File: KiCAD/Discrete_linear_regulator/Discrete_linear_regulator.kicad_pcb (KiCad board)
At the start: 2 copper layers, 50 x 30 mm, 14 parts, among them J1 Conn_01x06, Q1 PZT2222AT3G, Q2 BC857, Q3 BC857, Q4 PZT2222AT3G, Q5 PZT2907AT3G, Q6 BC847, Q7 BC847, Q8 PZT2907AT3G, U1 LM4562

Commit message: Worked a bit on the main board
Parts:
- added C1: 100nF, Capacitor_SMD:C_0402_1005Metric, B.Cu at (75.0, 64.0)
- added C3: 100nF, Capacitor_SMD:C_0402_1005Metric, B.Cu at (75.0, 66.0)
- moved Q6 90.0 mm to (97.1, 69.5)
- moved Q7 90.0 mm to (97.1, 74.0)
- moved C2 53.3 mm to (81.0, 63.0)
- moved Q2 52.8 mm to (62.0, 65.0), turned to 180 degrees
- moved R2 52.5 mm to (61.0, 72.0), turned to 90 degrees
- moved Q3 52.4 mm to (62.0, 69.0), turned to 90 degrees
- moved R1 49.3 mm to (65.0, 65.0), turned to -90 degrees
- moved C4 46.8 mm to (69.0, 66.0), turned to 180 degrees

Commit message: sepic step file
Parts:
- removed Q6, Q7: BC847, Package_TO_SOT_SMD:SOT-23
- added C10: 100u, Capacitor_THT:CP_Radial_D8.0mm_P3.50mm, F.Cu at (39.8, 92.3)
- added C11: 100u, Capacitor_THT:CP_Radial_D8.0mm_P3.50mm, F.Cu at (110.8, 56.0)
- added C12: 100u, Capacitor_THT:CP_Radial_D8.0mm_P3.50mm, F.Cu at (110.8, 65.5)
- added C13: 10u, Capacitor_SMD:C_1210_3225Metric, F.Cu at (38.1, 64.2)
- added C14: 100n, Capacitor_SMD:C_0402_1005Metric, F.Cu at (42.3, 62.7)
- added C15: 100p, Capacitor_SMD:C_0402_1005Metric, F.Cu at (42.3, 64.7)
- added C16: 100u, Capacitor_THT:CP_Radial_D8.0mm_P3.50mm, F.Cu at (110.8, 75.0)
- added C5: 100u, Capacitor_THT:CP_Radial_D8.0mm_P3.50mm, F.Cu at (39.8, 73.2)
- added C6: 100u, Capacitor_THT:CP_Radial_D8.0mm_P3.50mm, F.Cu at (39.8, 82.8)
- added C9: 10u, Capacitor_SMD:C_1210_3225Metric, F.Cu at (38.1, 59.9)
- added Q10: BC857, Package_TO_SOT_SMD:SOT-23, F.Cu at (37.7, 43.2)
- added Q11: BC857, Package_TO_SOT_SMD:SOT-23, F.Cu at (37.7, 47.6)
- added R10: 47R, Resistor_SMD:R_0402_1005Metric, F.Cu at (39.6, 56.8)
- added R11: 10k, Resistor_SMD:R_0402_1005Metric, F.Cu at (42.5, 50.8)
- added R12: 780R, Resistor_SMD:R_0402_1005Metric, F.Cu at (42.5, 52.8)
- added R13: 8k2, Resistor_SMD:R_0402_1005Metric, F.Cu at (42.5, 54.8)
- added R14: 2k4, Resistor_SMD:R_0402_1005Metric, F.Cu at (42.5, 56.8)
- added R3: 47R, Resistor_SMD:R_0402_1005Metric, F.Cu at (36.7, 50.8)
- added R4: 100R, Resistor_SMD:R_0402_1005Metric, F.Cu at (36.7, 52.8)
- added R5: 100k, Resistor_SMD:R_0402_1005Metric, F.Cu at (36.7, 54.8)
- added R6: 8k2, Resistor_SMD:R_0402_1005Metric, F.Cu at (36.7, 56.8)
- added R7: 2k4, Resistor_SMD:R_0402_1005Metric, F.Cu at (39.6, 50.8)
- added R8: 100R, Resistor_SMD:R_0402_1005Metric, F.Cu at (39.6, 52.8)
- added R9: 100k, Resistor_SMD:R_0402_1005Metric, F.Cu at (39.6, 54.8)
- C4: value 100p -> 100n
- moved J1 6.00 mm to (81.3, 81.6)
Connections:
- C2 pad 1: unconnected-(C2-Pad1) -> Net-(U1A--)
- C2 pad 2: unconnected-(C2-Pad2) -> Net-(C2-Pad2)
- Q1 pad 1: unconnected-(Q1-Pad1) -> Net-(C6-Pad1)
- Q4 pad 1: Net-(Q4-Pad1) -> Net-(C2-Pad2)
- Q5 pad 1: unconnected-(Q5-Pad1) -> Net-(C15-Pad2)
- Q5 pad 2: unconnected-(Q5-Pad2) -> Net-(Q10-E)
- Q5 pad 3: unconnected-(Q5-Pad3) -> -12V
- Q5 pad 4: unconnected-(Q5-Pad4) -> Net-(Q10-E)
- Q8 pad 1: unconnected-(Q8-Pad1) -> Net-(C12-Pad2)
- Q8 pad 2: unconnected-(Q8-Pad2) -> -15V
- Q8 pad 3: unconnected-(Q8-Pad3) -> Net-(Q10-E)
- Q8 pad 4: unconnected-(Q8-Pad4) -> -15V
- U1 pad 1: Net-(Q4-Pad1) -> Net-(C2-Pad2)
- U1 pad 2: unconnected-(U1A---Pad2) -> Net-(U1A--)
- U1 pad 5: unconnected-(U1B-+-Pad5) -> Net-(D3-K)
- U1 pad 6: unconnected-(U1B---Pad6) -> Net-(U1B--)
- U1 pad 7: unconnected-(U1-Pad7) -> Net-(C15-Pad2)
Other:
- board size 50 x 30 mm -> 50 x 36 mm

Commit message: update SDD front/back end
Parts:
- moved R10 84.6 mm to (124.2, 55.9)
- moved R9 82.9 mm to (122.5, 56.4), turned to 90 degrees
- moved R8 82.9 mm to (122.5, 54.3), turned to -90 degrees
- moved C13 67.5 mm to (105.6, 65.5)
- moved Q10 56.9 mm to (89.8, 66.2), turned to 180 degrees
- moved Q11 56.6 mm to (89.8, 69.8), turned to 90 degrees
- moved J1 55.7 mm to (35.8, 113.8)
- moved R12 51.6 mm to (92.4, 66.1), turned to -90 degrees
- moved R11 51.2 mm to (88.8, 72.8), turned to 90 degrees
- moved C14 37.7 mm to (79.8, 66.9)
- moved C15 37.0 mm to (79.3, 65.1), turned to 90 degrees
- moved R7 36.6 mm to (61.2, 80.3), turned to -90 degrees
- moved R6 32.5 mm to (61.3, 78.0), turned to -90 degrees
- moved C16 31.4 mm to (79.4, 76.5)
- moved R14 31.1 mm to (62.9, 80.3), turned to -90 degrees
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
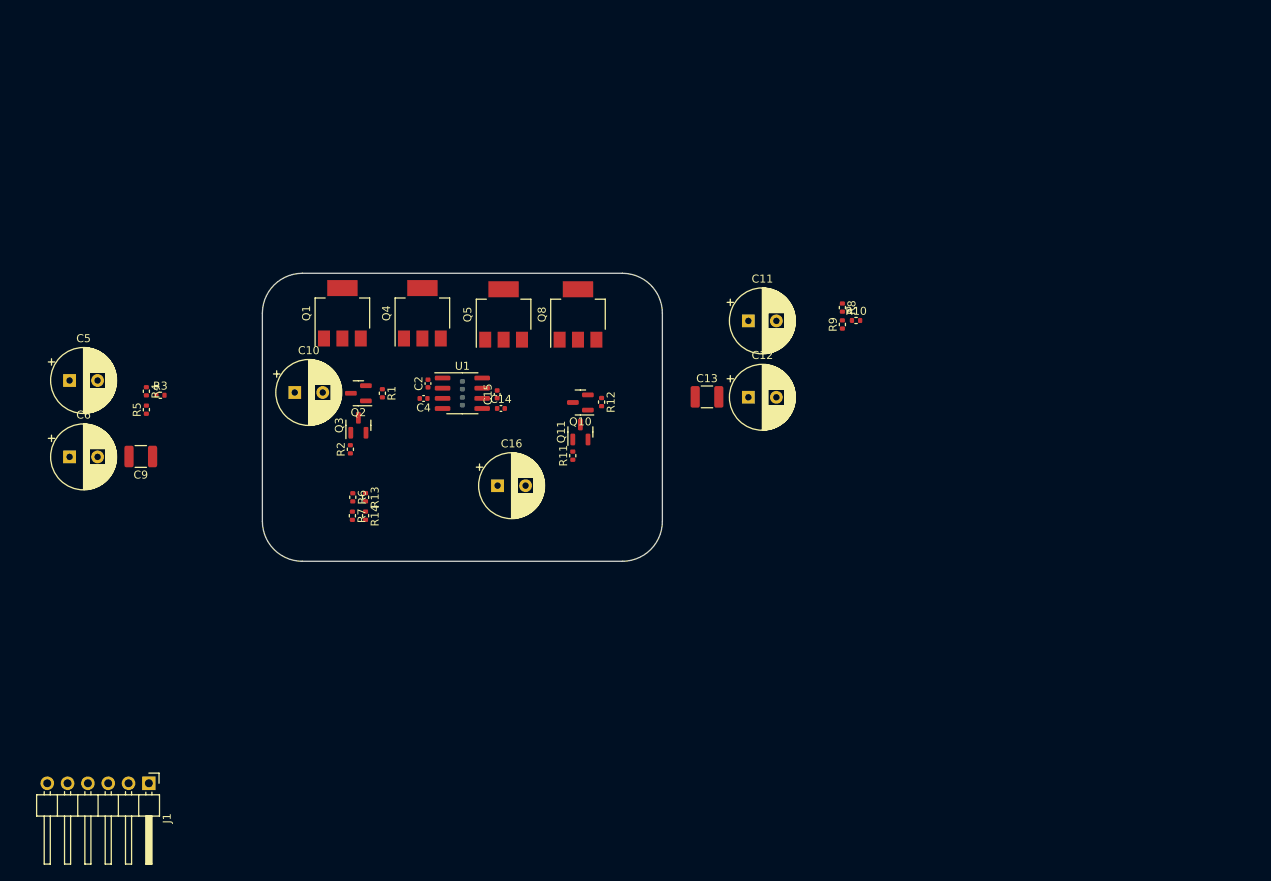
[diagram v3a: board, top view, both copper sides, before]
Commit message: linear regulators changes
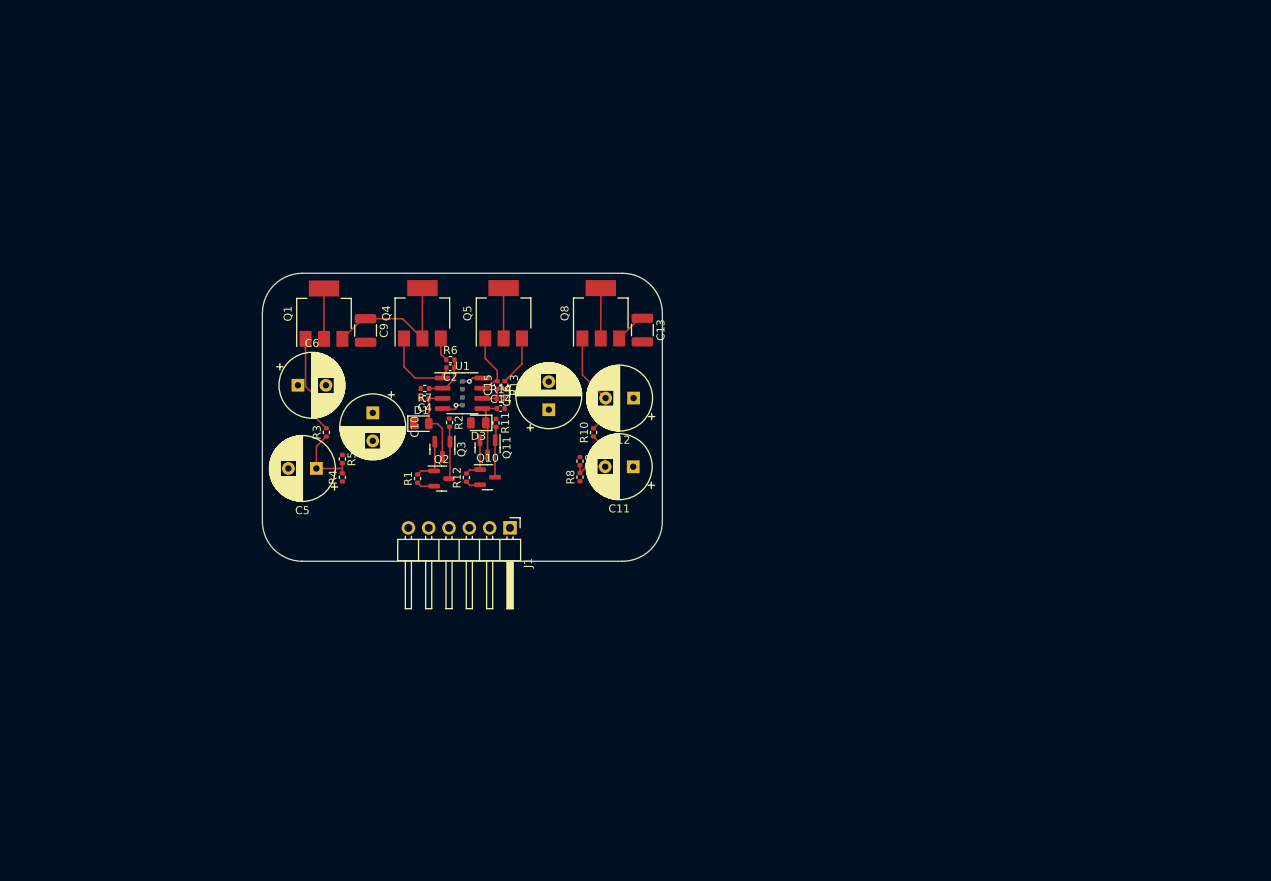
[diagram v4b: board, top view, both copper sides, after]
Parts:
- added D1: LED, LED_SMD:LED_0805_2012Metric, F.Cu at (69.9, 68.8)
- added D3: LED, LED_SMD:LED_0805_2012Metric, F.Cu at (77.0, 68.7)
- moved J1 55.3 mm to (81.0, 81.8)
- moved R8 39.1 mm to (89.7, 75.5), turned to 90 degrees
- moved R9 37.0 mm to (89.7, 73.5), turned to -90 degrees
- moved R10 35.7 mm to (91.4, 69.9), turned to 90 degrees
- moved C5 32.8 mm to (56.8, 74.4), turned to 180 degrees
- moved C9 32.2 mm to (62.9, 57.1), turned to -90 degrees
- moved C6 29.9 mm to (54.4, 64.0)
- moved R4 26.8 mm to (60.0, 75.5), turned to 90 degrees
- moved R5 25.3 mm to (60.0, 73.2), turned to -90 degrees
- moved C11 23.2 mm to (96.4, 74.2), turned to 180 degrees
- moved R13 22.3 mm to (80.3, 64.0)
- moved R14 22.3 mm to (79.8, 65.7), turned to 0 degrees
- moved R3 21.3 mm to (58.0, 69.9), turned to 90 degrees
- moved R6 21.1 mm to (73.5, 60.8), turned to 0 degrees
- moved R12 19.4 mm to (75.5, 75.5), turned to 90 degrees
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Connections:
- J1 pad 1: +15V -> -15V
- J1 pad 3: +12V -> -12V
- J1 pad 4: -12V -> +12V
- J1 pad 6: -15V -> +15V
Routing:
- net Net-(Q2-E): track 0.00 -> 20.6 mm
- net Net-(C12-Pad2): track 0.00 -> 13.1 mm
- net Net-(C6-Pad1): track 0.00 -> 12.3 mm
- net Net-(Q10-E): track 0.00 -> 12.2 mm
- net Net-(C2-Pad2): track 0.00 -> 10.4 mm
- net Net-(D1-A): track 0.00 -> 10.4 mm
- net Net-(C5-Pad1): track 0.00 -> 9.04 mm
- net Net-(C11-Pad2): track 0.00 -> 8.84 mm
- net Net-(C15-Pad2): track 0.00 -> 8.49 mm
- net Net-(D3-K): track 0.00 -> 8.10 mm
- net Net-(Q2-C): track 0.00 -> 6.56 mm
- net Net-(Q10-C): track 0.00 -> 6.31 mm
- net +15V: track 0.00 -> 6.30 mm
- net -15V: track 0.00 -> 6.30 mm
- net -12V: track 0.00 -> 6.22 mm
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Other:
- copper layers 2 -> 4

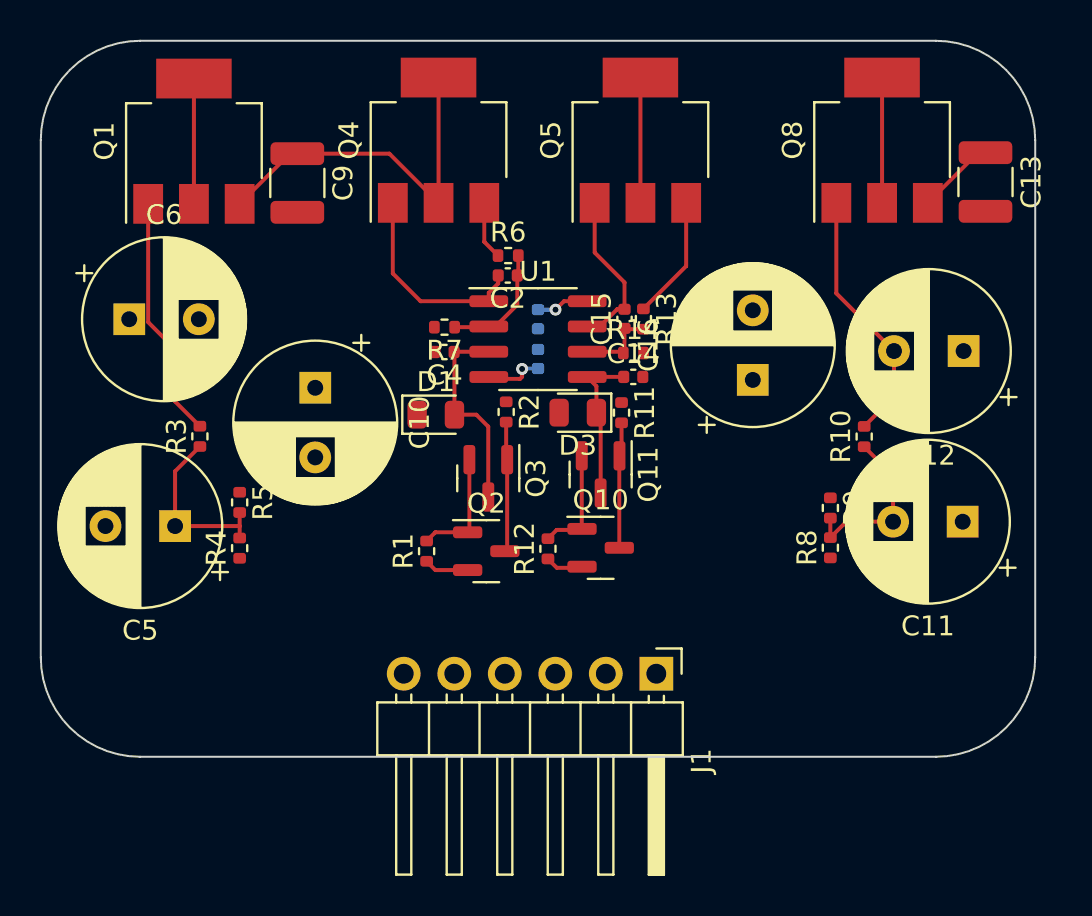
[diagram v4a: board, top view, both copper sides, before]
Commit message: update linear regulator pcb
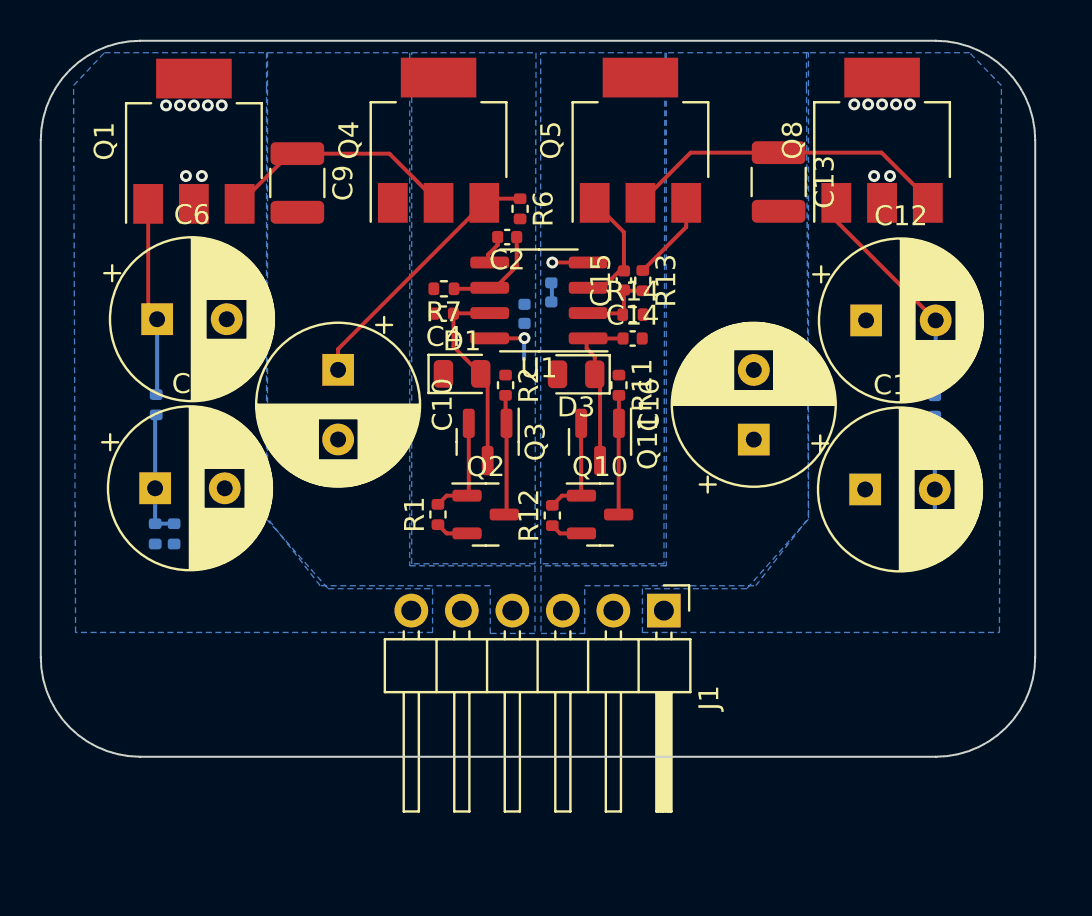
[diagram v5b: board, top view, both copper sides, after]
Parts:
- R10, R3, R4, R5, R8, R9: moved to B.Cu
- moved C13 10.4 mm to (87.1, 57.1)
- moved R8 5.25 mm to (94.9, 74.8)
- moved C11 5.16 mm to (91.5, 72.6), turned to 0 degrees
- moved C12 5.14 mm to (91.5, 64.1), turned to 0 degrees
- moved R9 4.44 mm to (94.0, 74.8), turned to 90 degrees
- moved R4 4.31 mm to (55.8, 74.8)
- moved R10 3.87 mm to (95.0, 68.4)
- moved R5 3.66 mm to (56.7, 74.8), turned to 90 degrees
- moved C3 3.42 mm to (75.7, 62.6), turned to 90 degrees
- moved J1 3.20 mm to (81.3, 78.7)
- moved C16 3.00 mm to (85.8, 70.1)
- moved R3 2.71 mm to (55.8, 68.3)
- moved D1 2.44 mm to (71.2, 66.8)
- moved R6 2.43 mm to (74.1, 58.5), turned to -90 degrees
- moved C5 2.15 mm to (55.8, 72.5), turned to 0 degrees
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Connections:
- C1 pad 1: Net-(U1C-V+) -> V+
- C13 pad 1: Net-(Q10-E) -> V-
- C15 pad 1: Net-(U1B--) -> Net-(U1A-+)
- C2 pad 1: Net-(U1A--) -> Net-(U1B-+)
- C3 pad 2: Net-(U1C-V-) -> V-
- C9 pad 1: Net-(Q2-E) -> V+
- Q1 pad 3: Net-(Q2-E) -> V+
- Q10 pad 2: Net-(Q10-E) -> V-
- Q2 pad 2: Net-(Q2-E) -> V+
- Q4 pad 2: Net-(Q2-E) -> V+
- Q4 pad 4: Net-(Q2-E) -> V+
- Q5 pad 2: Net-(Q10-E) -> V-
- Q5 pad 4: Net-(Q10-E) -> V-
- Q8 pad 3: Net-(Q10-E) -> V-
- R1 pad 1: Net-(Q2-E) -> V+
- R12 pad 1: Net-(Q10-E) -> V-
- R13 pad 2: Net-(U1B--) -> Net-(U1A-+)
- R14 pad 1: Net-(U1B--) -> Net-(U1A-+)
- R6 pad 2: Net-(U1A--) -> Net-(U1B-+)
- R7 pad 1: Net-(U1A--) -> Net-(U1B-+)
- U1 pad 1: Net-(C2-Pad2) -> Net-(C15-Pad2)
- U1 pad 2: Net-(U1A--) -> Net-(D3-K)
- U1 pad 3: Net-(D1-A) -> Net-(U1A-+)
- U1 pad 4: Net-(U1C-V-) -> V-
- U1 pad 5: Net-(D3-K) -> Net-(U1B-+)
- U1 pad 6: Net-(U1B--) -> Net-(D1-A)
- U1 pad 7: Net-(C15-Pad2) -> Net-(C2-Pad2)
- U1 pad 8: Net-(U1C-V+) -> V+
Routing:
- net V-: track 0.00 -> 21.2 mm, vias 0 -> 1
- net Net-(Q2-E): track 20.6 -> 0.00 mm
- net V+: track 0.00 -> 16.3 mm, vias 0 -> 1
- net Net-(Q10-E): track 12.2 -> 0.00 mm
- net +12V: track 2.94 -> 13.3 mm
- net Net-(C2-Pad2): track 10.4 -> 1.49 mm
- net +15V: track 6.30 -> 0.00 mm, vias 0 -> 6
- net -15V: track 6.30 -> 0.00 mm, vias 0 -> 8
- net Net-(U1A--): track 6.11 -> 0.00 mm
- net Net-(U1B-+): track 0.00 -> 5.16 mm
- net Net-(U1B--): track 4.46 -> 0.00 mm
- net Net-(U1A-+): track 0.00 -> 4.46 mm
- net Net-(U1C-V-): track 2.96 -> 0.00 mm, vias 1 -> 0
- net Net-(U1C-V+): track 2.68 -> 0.00 mm, vias 1 -> 0
- net Net-(C5-Pad1): track 9.04 -> 6.44 mm
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- added copper zone on B.Cu, net +12V
- added copper zone on B.Cu, net +15V
- added copper zone on B.Cu, net -12V
- added copper zone on B.Cu, net -15V
- added copper zone on B.Cu, net V+
- added copper zone on B.Cu, net V-

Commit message: update linear regulators
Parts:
- Q4, Q8: moved to B.Cu
- moved C9 81.0 mm to (137.9, 87.6)
- moved Q8 80.5 mm to (166.8, 85.5)
- moved C3 80.1 mm to (149.8, 93.1)
- moved C1 80.1 mm to (148.4, 94.2)
- moved C11 80.1 mm to (165.5, 103.1)
- moved C12 80.1 mm to (165.5, 94.6)
- moved C16 80.1 mm to (159.9, 100.5)
- moved D3 80.1 mm to (151.0, 97.3)
- moved J1 80.1 mm to (155.4, 109.1)
- moved Q1 80.1 mm to (131.8, 85.5)
- moved Q3 80.1 mm to (146.5, 100.7)
- moved Q4 80.1 mm to (144.1, 85.5)
- moved R1 80.1 mm to (144.0, 104.3)
- moved R10 80.1 mm to (169.0, 98.9)
- moved R11 80.1 mm to (153.1, 97.8)
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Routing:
- net V-: track 21.2 -> 4.54 mm, vias 1 -> 8
- net +12V: track 13.3 -> 0.00 mm
- net V+: track 16.3 -> 8.22 mm
- net Net-(C15-Pad2): track 6.55 -> 0.16 mm
- net Net-(U1B-+): track 5.16 -> 0.00 mm
- net Net-(D1-A): track 9.88 -> 4.89 mm
- net -12V: track 4.30 -> 0.00 mm
- net Net-(D3-K): track 8.40 -> 4.59 mm
- net Net-(U1A-+): track 4.46 -> 1.08 mm
- net Net-(C12-Pad2): track 11.8 -> 9.72 mm
- net Net-(C2-Pad2): track 1.49 -> 0.00 mm
- net -15V: vias 8 -> 0
- net +15V: vias 6 -> 7
- added copper zone on F.Cu, net +15V
- added copper zone on F.Cu, net V-

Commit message: linear
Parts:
- moved C9 6.72 mm to (144.0, 84.7), turned to 90 degrees
- moved R9 6.55 mm to (163.9, 110.4)
- moved R8 6.55 mm to (164.9, 110.4)
- moved R5 5.49 mm to (133.7, 109.6)
- moved C5 5.48 mm to (132.8, 107.2)
- moved R4 5.38 mm to (132.6, 109.6)
- moved C11 5.25 mm to (162.3, 107.2)
- moved R3 3.87 mm to (132.8, 100.7)
- moved Q1 3.85 mm to (135.6, 85.5)
- moved C6 3.30 mm to (132.8, 94.4)
- moved R10 3.28 mm to (166.1, 100.4)
- moved C12 3.15 mm to (162.4, 94.4)
- moved Q8 3.15 mm to (163.6, 85.5)
- moved C10 2.50 mm to (140.1, 99.0)
- moved C16 2.39 mm to (158.6, 102.6)
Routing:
- net Net-(C6-Pad1): track 10.3 -> 0.00 mm
- net Net-(C12-Pad2): track 9.72 -> 0.00 mm
- net Net-(C5-Pad1): track 6.44 -> 0.00 mm
- net Net-(C11-Pad2): track 6.35 -> 0.00 mm
- net V+: track 8.22 -> 4.27 mm
- net V-: vias 8 -> 1
- net +15V: vias 7 -> 0
